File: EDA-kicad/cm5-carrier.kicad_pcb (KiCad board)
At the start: 2 copper layers, 80 x 150 mm, 44 parts, among them J1 SJ2-35894B-SMT-TR, J2 USBC-3-2-fix-USB4056-03-A_REV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, J3 SIM-G85D1160022HHR, J4 FINGER, SW1 CHP-041B, SW2 PROG, SW3 VOL-, SW4 VOL+, SW5 POW, U1 BAT-STEP-UP-MIC2876-5.0YMT-TR, U2 BAT-CONNECTOR-FLTS22WR00, U3 BAT-MONITOR-BQ27530YZFT-G1, U4 CHARGER-SWITCHER-BQ25303JRTER, U5 Flash-LED-Lumiled, U6 FPC15pin-1mm-pitch-F52Q-1A7H1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, U7 CODEC-TLV320AIC3204IRHBR, U8 DAC-TLV320DAC3100IRHBR, U9 GSM-GPS-EC25VFA-512-STD

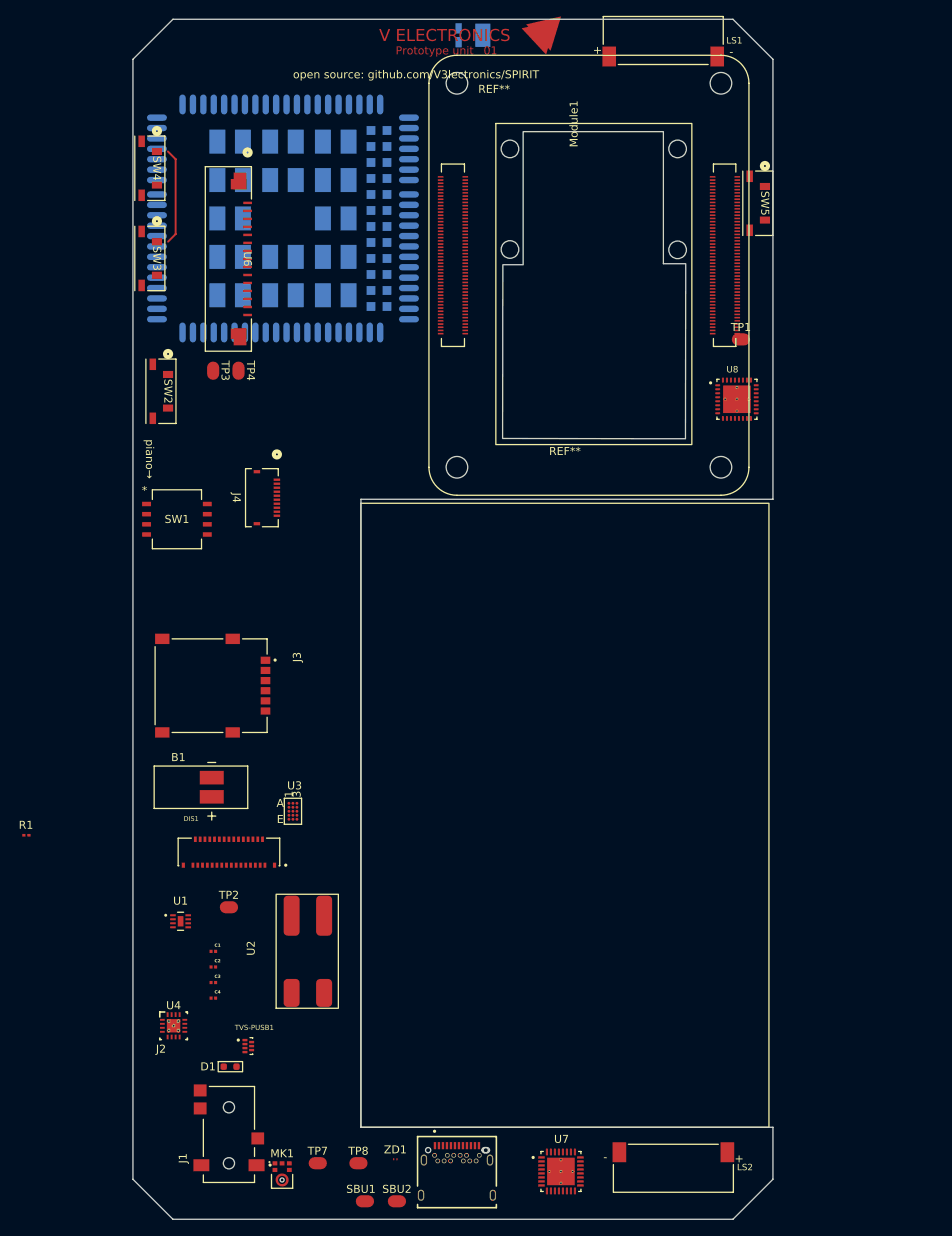
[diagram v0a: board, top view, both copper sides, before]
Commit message: flashlight and vibration MOSFET drivers
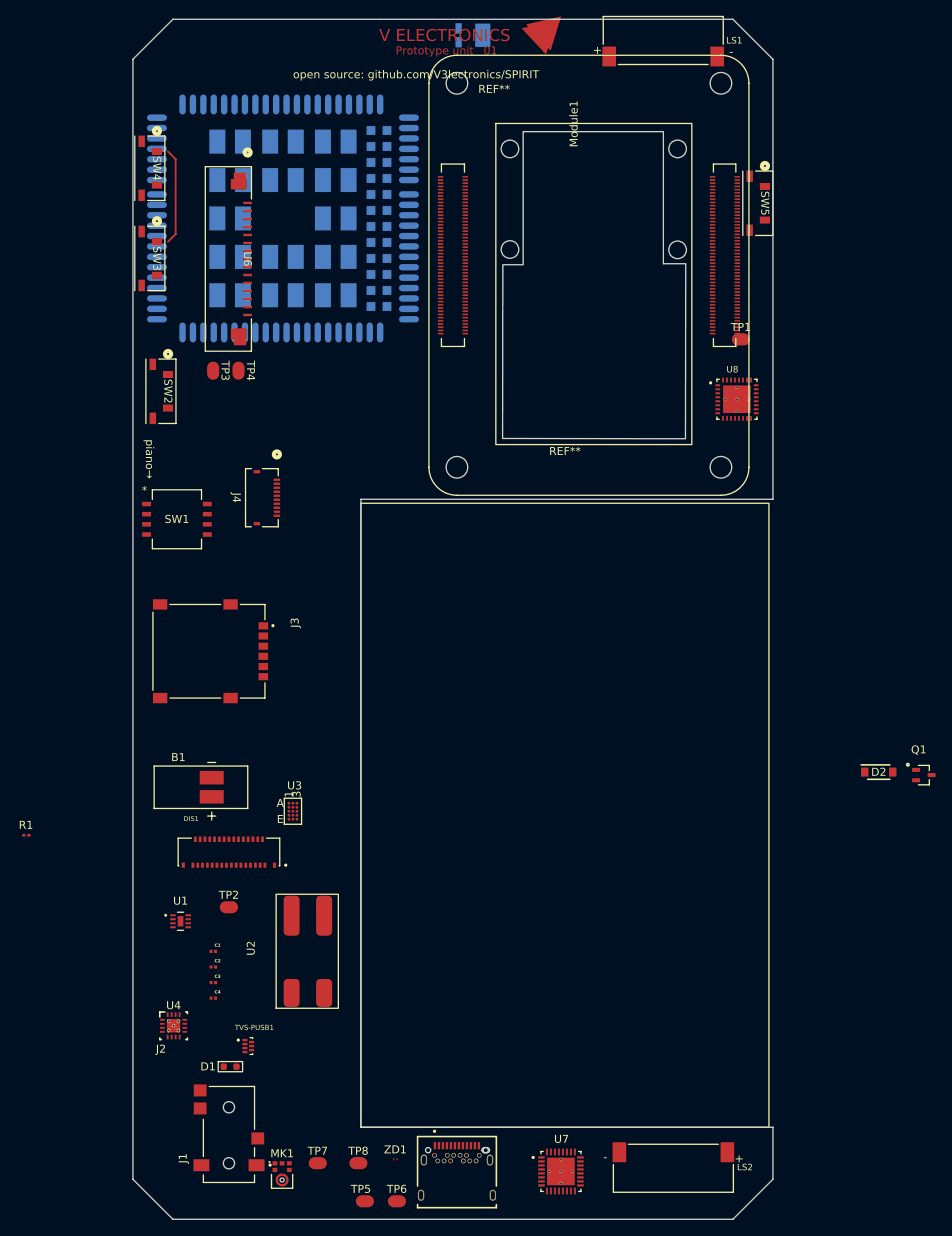
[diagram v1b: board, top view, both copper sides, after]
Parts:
- added D2: 1N4007W-T, SPIRIT-footprints:flyback-diode-SODFL3818X130N, F.Cu at (148.2, 125.1)
- added Q1: ~, SPIRIT-footprints:gpio-driver-transistor-fix-SOT65P210X110-3N, F.Cu at (153.9, 125.5)
- moved J3 4.31 mm to (64.5, 110.0)
- renumbered SBU1 to TP5, SBU2 to TP6
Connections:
- U5 pad 1: GND -> Net-(Q1-D)
- U5 pad 2: Net-(Module1A-GPIO22) -> VCC
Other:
- board text added: "for LED datasheet recommends a special layout for efficient thermal dissipation"

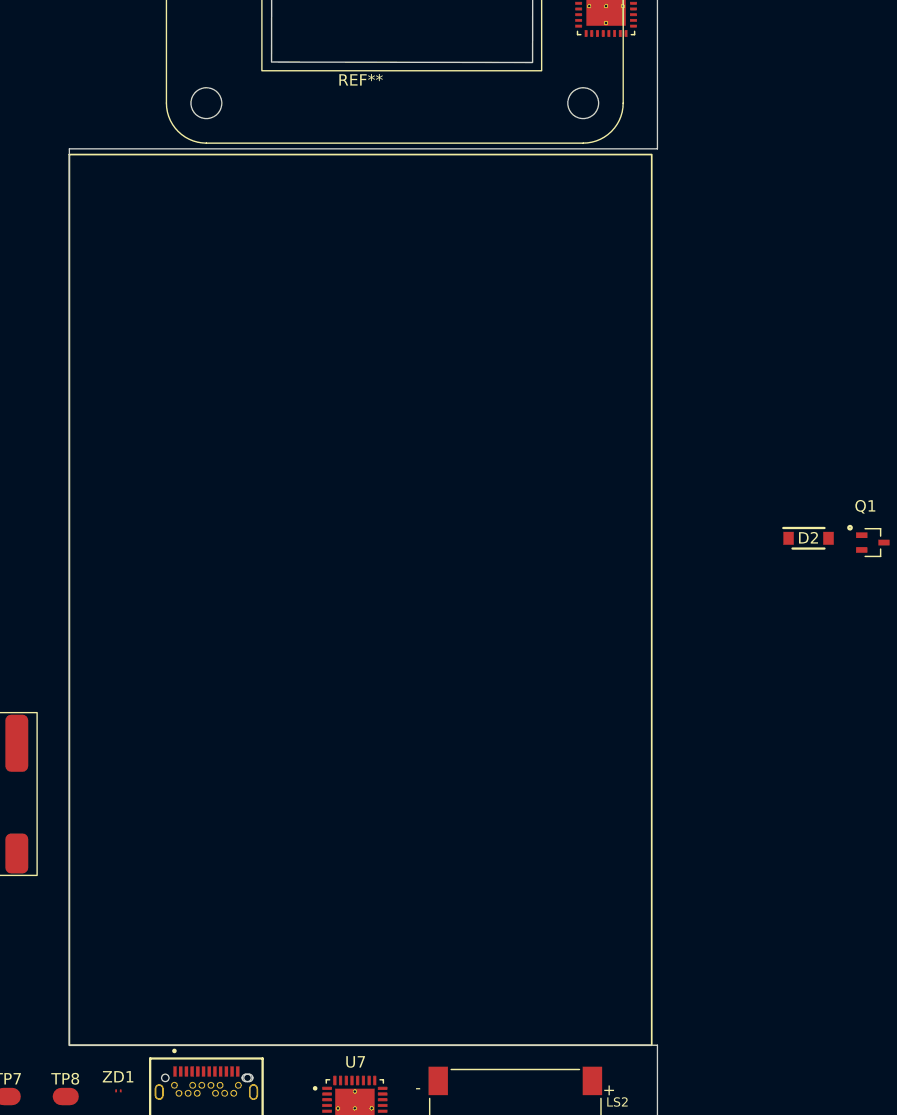
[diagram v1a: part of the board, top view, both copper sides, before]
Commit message: assign new 3500 mAh bat footprint to symbol
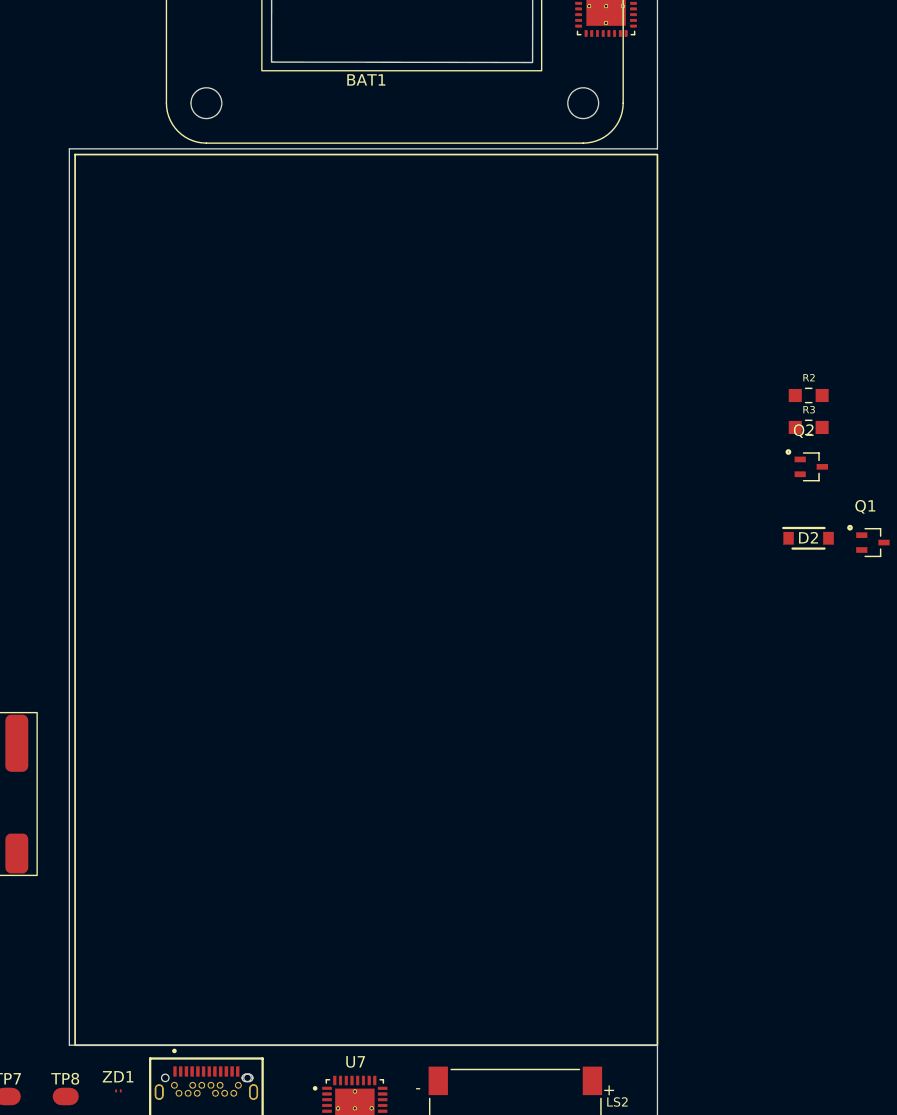
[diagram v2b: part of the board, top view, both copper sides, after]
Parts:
- removed the REF** at (109.0, 96.5)
- added BAT1: battery_37V3500mAhLP685077JU, SPIRIT-footprints:battery_37V3500mAhLP685077JU, F.Cu at (109.5, 96.5)
- added Q2: ~, SPIRIT-footprints:gpio-driver-transistor-fix-SOT65P210X110-3N, F.Cu at (148.5, 118.8)
- added R2: 1K-05W-0805-RES_ERJP06J102V, SPIRIT-footprints:1K-05W-0805-RES_ERJP06J102V, F.Cu at (148.2, 112.6)
- added R3: 1K-05W-0805-RES_ERJP06J102V, SPIRIT-footprints:1K-05W-0805-RES_ERJP06J102V, F.Cu at (148.2, 115.4)
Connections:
- B1 pad N: Net-(Module1A-GPIO27) -> Net-(Q2-D)
- B1 pad P: GND -> VCC
- D2 pad 1: unconnected-(D2-Pad1) -> VCC
- D2 pad 2: unconnected-(D2-Pad2) -> Net-(Q2-D)
- Q1 pad 1: Net-(Module1A-GPIO22) -> Net-(Q1-G)
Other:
- board text added: "led, motor drivers circuitry"

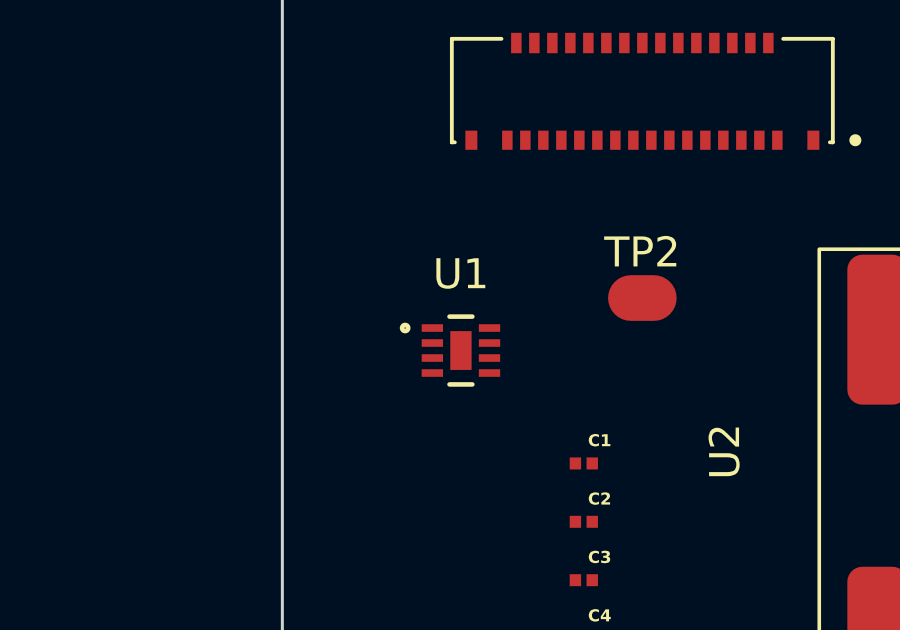
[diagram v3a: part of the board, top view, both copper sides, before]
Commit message: Power system is finally working, i hope so atleast. Issues are the syme as gefore (2 resistors missing values and a missing BATFET connection, but everything is marked so it should be easy to find
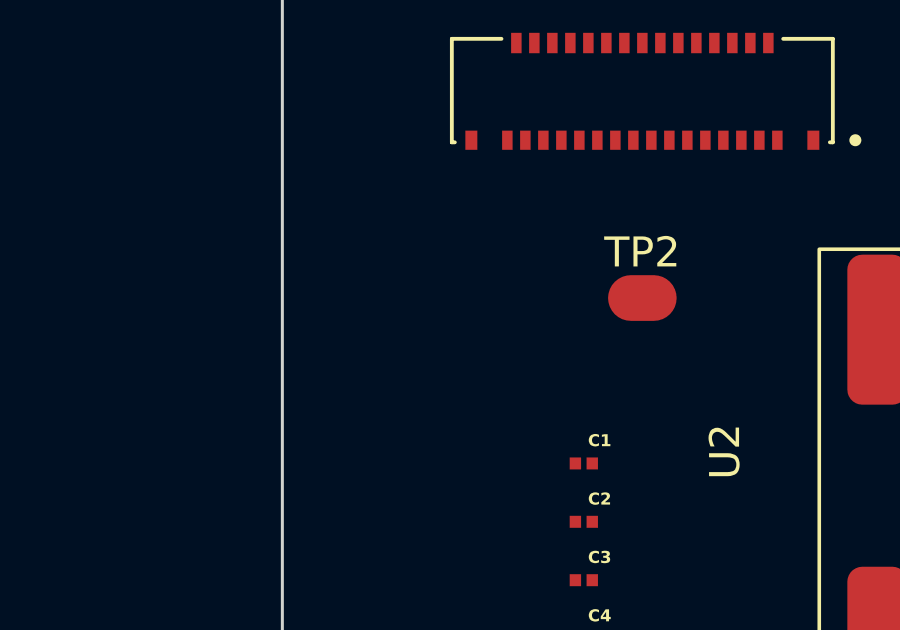
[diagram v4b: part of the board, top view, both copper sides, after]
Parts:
- removed U1: BAT-STEP-UP-MIC2876-5.0YMT-TR, SPIRIT-footprints:BAT-STEP-UP-UDFN8_2X2_MCH

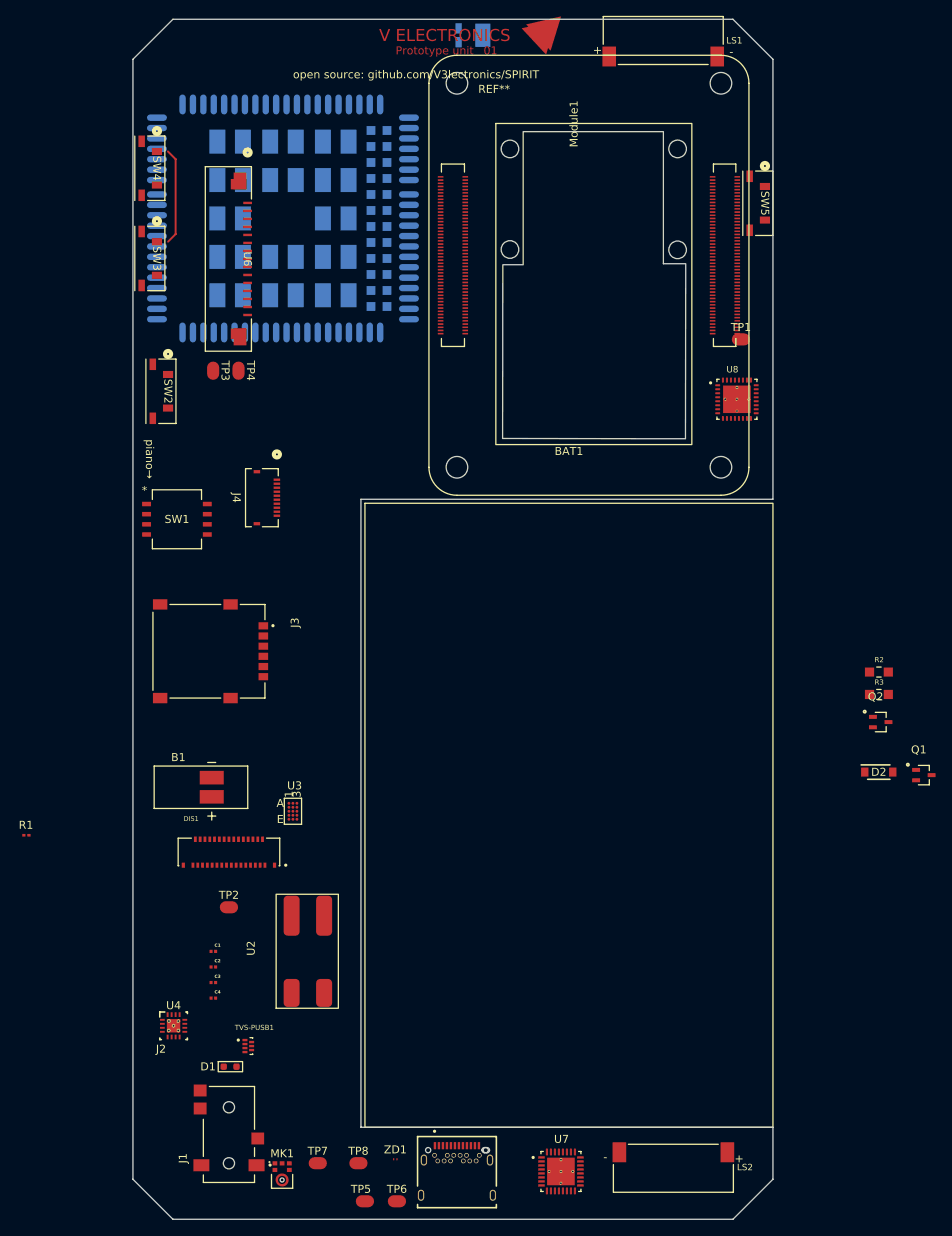
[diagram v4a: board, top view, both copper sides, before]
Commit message: fix'ed 3D models
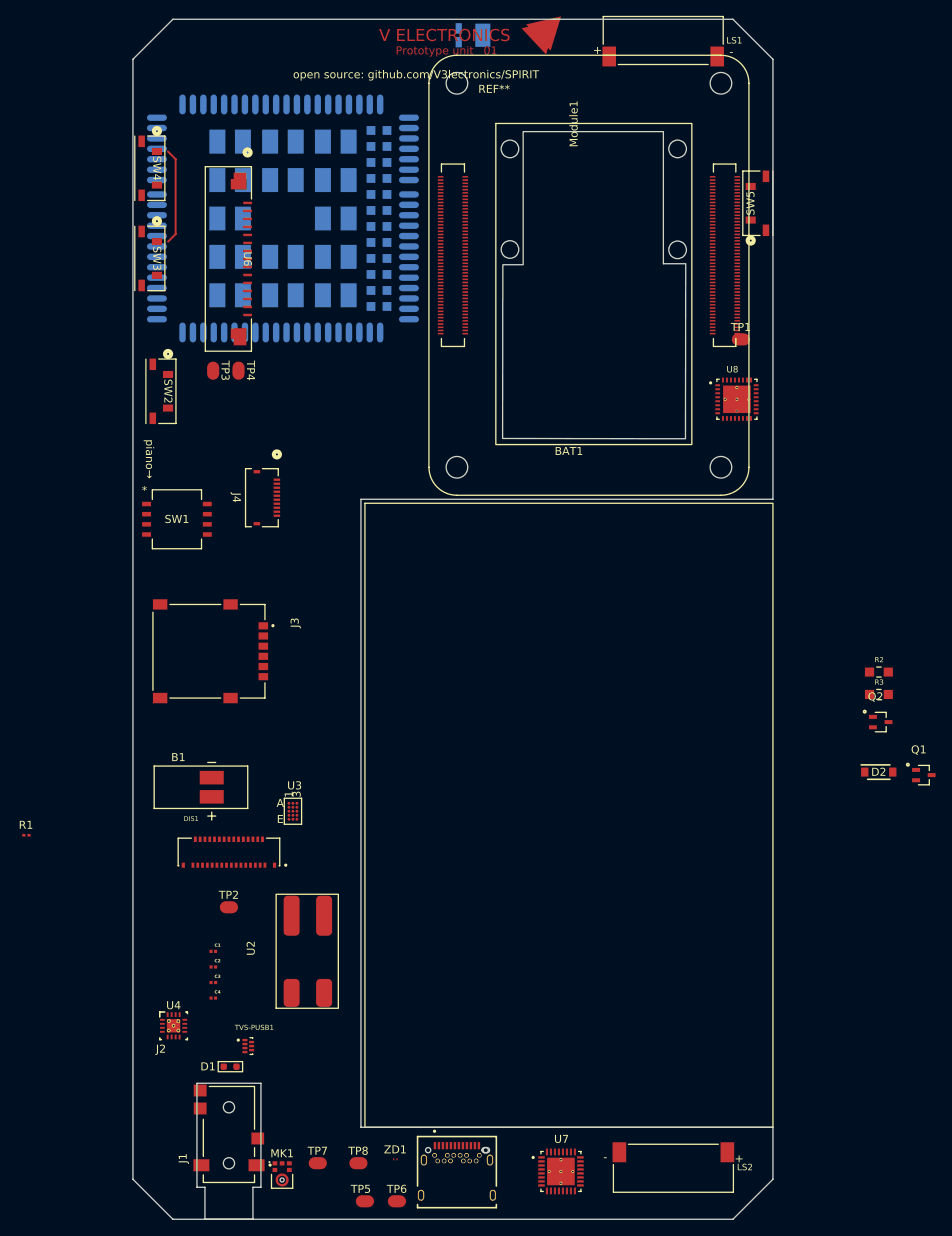
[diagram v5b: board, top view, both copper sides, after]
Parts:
- turned SW5 to 90 degrees
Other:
- outline, holes or cut-outs redrawn
